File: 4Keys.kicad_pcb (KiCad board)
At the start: 2 copper layers, 103.2 x 52.4 mm, 29 parts, among them J1 OLED1, J2 OLED2, SW1 SW_Reset, U1 ATmega32U4-AU, Y1 16MHz

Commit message: Hotswap
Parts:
- MXDn1, MXLeft1, MXRight1, MXUp1: footprint MX_Alps_Hybrid:MX-1U-NoLED -> MX_Only:MXOnly-1U-Hotswap
- moved C6 23.5 mm to (202.7, 41.1)
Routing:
- net SCL: track 88.3 -> 139.4 mm, vias 0 -> 3
- net SDA: track 89.0 -> 137.7 mm, vias 0 -> 1
- net col1: track 44.5 -> 51.2 mm, vias 1 -> 3
- net col2: track 6.74 -> 0.40 mm, vias 1 -> 0
- net Net-(D4-Pad2): track 5.61 -> 0.00 mm
- net +5V: track 208.8 -> 214.1 mm
- net col0: track 50.7 -> 54.6 mm, vias 1 -> 2
- net row1: track 41.3 -> 44.4 mm
- net (no net): track 0.00 -> 2.98 mm, vias 0 -> 1
- net Net-(D3-Pad2): track 5.61 -> 5.81 mm, vias 0 -> 1
- net Net-(D5-Pad2): track 5.75 -> 5.71 mm, vias 0 -> 1

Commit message: Update PCB
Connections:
- U1 pad 10: Net-(U1-Pad10) -> row1
- U1 pad 30: row1 -> Net-(U1-Pad30)
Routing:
- net GND: track 27.9 -> 48.3 mm
- net +5V: track 214.1 -> 222.0 mm
- net col2: track 0.40 -> 6.81 mm
- net Net-(D4-Pad2): track 0.00 -> 5.81 mm, vias 0 -> 1
- net row1: track 44.4 -> 48.6 mm, vias 0 -> 1
- net col1: track 51.2 -> 48.1 mm, vias 3 -> 2
- net (no net): track 2.98 -> 0.00 mm, vias 1 -> 0
- net Net-(D2-Pad2): track 5.61 -> 4.24 mm, vias 0 -> 1

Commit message: Update PCB
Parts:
- moved C6 18.7 mm to (191.8, 56.3), turned to 90 degrees
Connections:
- U1 pad 22: Net-(U1-Pad22) -> col0
- U1 pad 29: col0 -> Net-(U1-Pad29)
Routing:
- net GND: track 48.3 -> 143.2 mm, vias 0 -> 9
- net +5V: track 222.0 -> 270.7 mm, vias 2 -> 6
- net Net-(R3-Pad2): track 12.9 -> 25.4 mm
- net col0: track 54.6 -> 52.4 mm, vias 2 -> 0
- added copper zone on B.Cu, net GND
- added copper zone on F.Cu, net GND

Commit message: Updqte PCB V1
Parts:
- moved J2 3.29 mm to (227.6, 74.6)
- moved J1 3.05 mm to (136.7, 74.6)
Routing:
- net GND: track 143.2 -> 59.0 mm, vias 9 -> 5
- net SDA: track 137.7 -> 145.7 mm
- net SCL: track 139.4 -> 147.3 mm
- net +5V: track 270.7 -> 272.0 mm, vias 6 -> 7
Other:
- board size 103.2 x 52.4 mm -> 124.8 x 52.4 mm

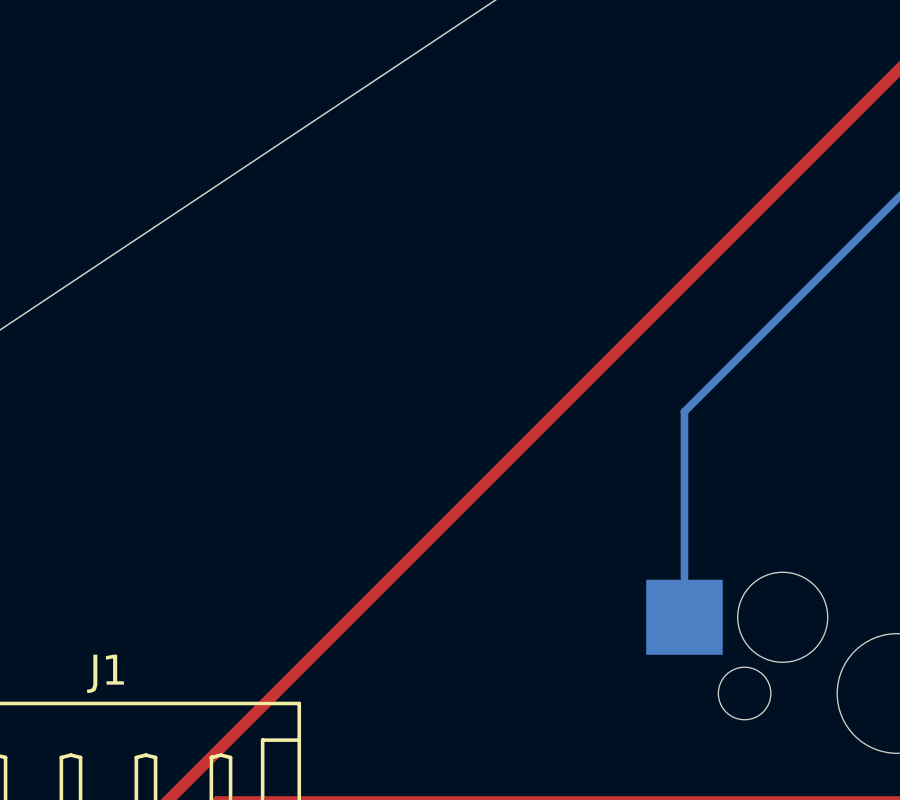
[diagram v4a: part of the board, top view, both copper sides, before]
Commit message: Updqte logo CC
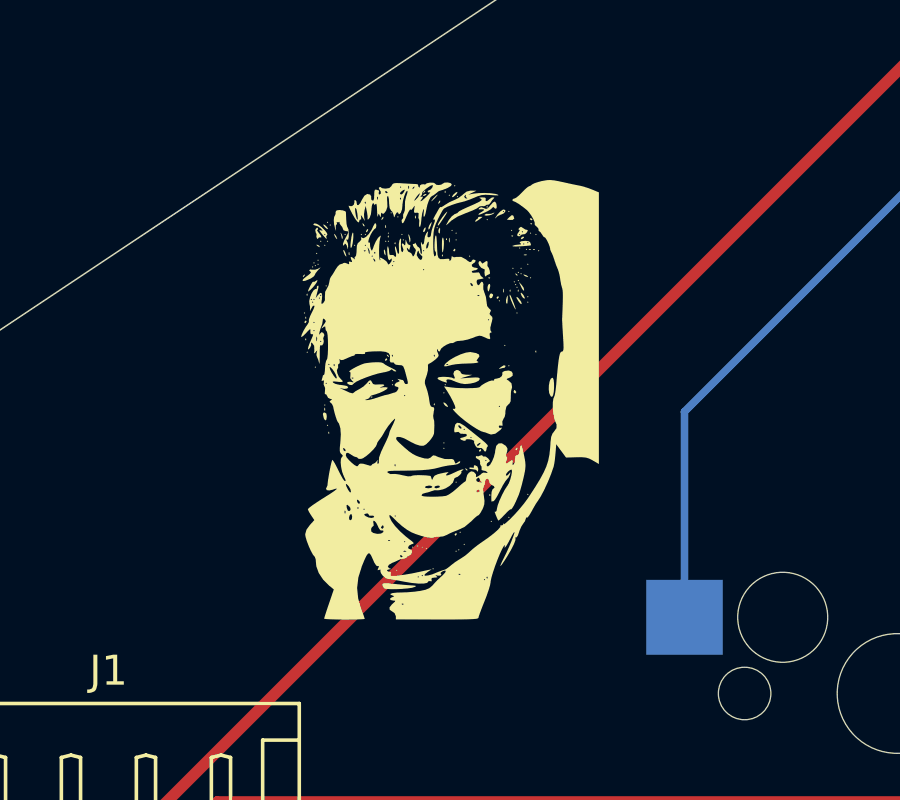
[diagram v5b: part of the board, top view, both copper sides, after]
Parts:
- added G***: LOGO, MX_Only:cc, F.Cu at (151.1, 57.5)

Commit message: Update PCB
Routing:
- net row1: track 48.6 -> 48.0 mm
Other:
- outline, holes or cut-outs redrawn
